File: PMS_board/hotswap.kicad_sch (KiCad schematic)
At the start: 18 parts, among them Q1 Q_NMOS_GDS, Q2 Q_NMOS_GDS, Q3 Q_NMOS_GDS, Q4 Q_NMOS_GDS, U6 LM74800QDRRRQ1, U7 LM74800QDRRRQ1

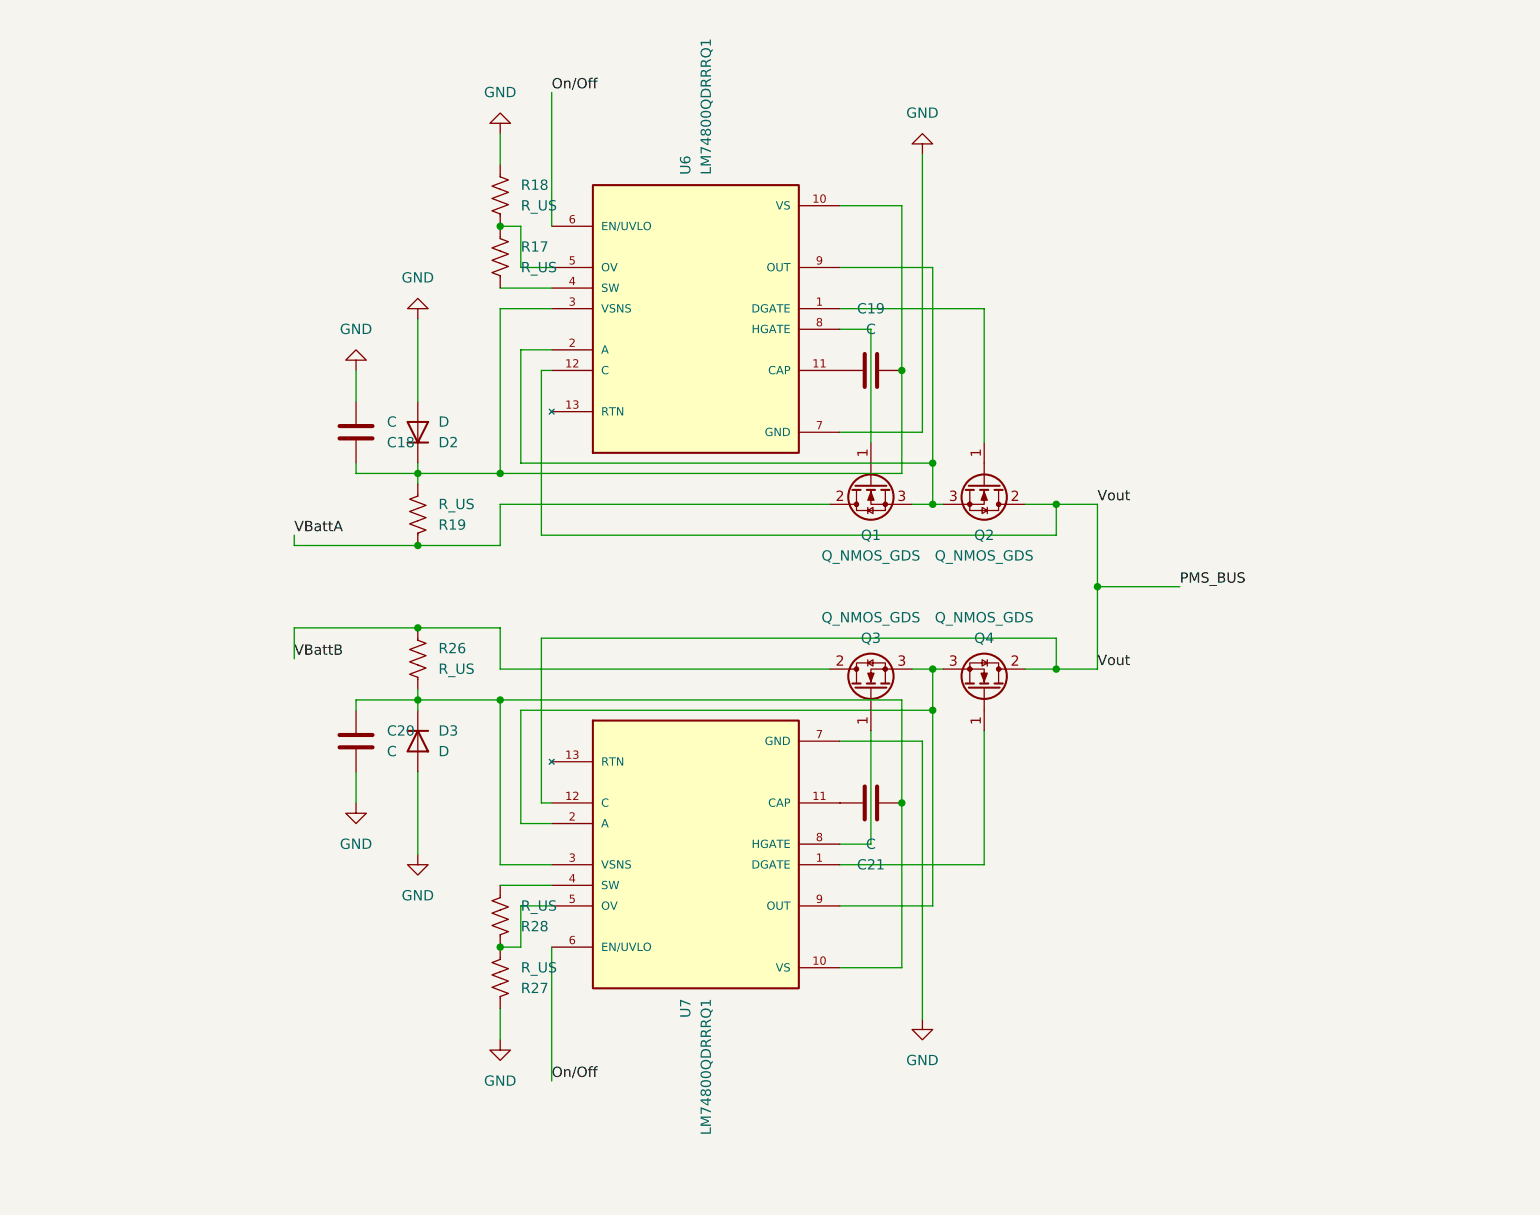
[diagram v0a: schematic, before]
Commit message: Added extra sheets
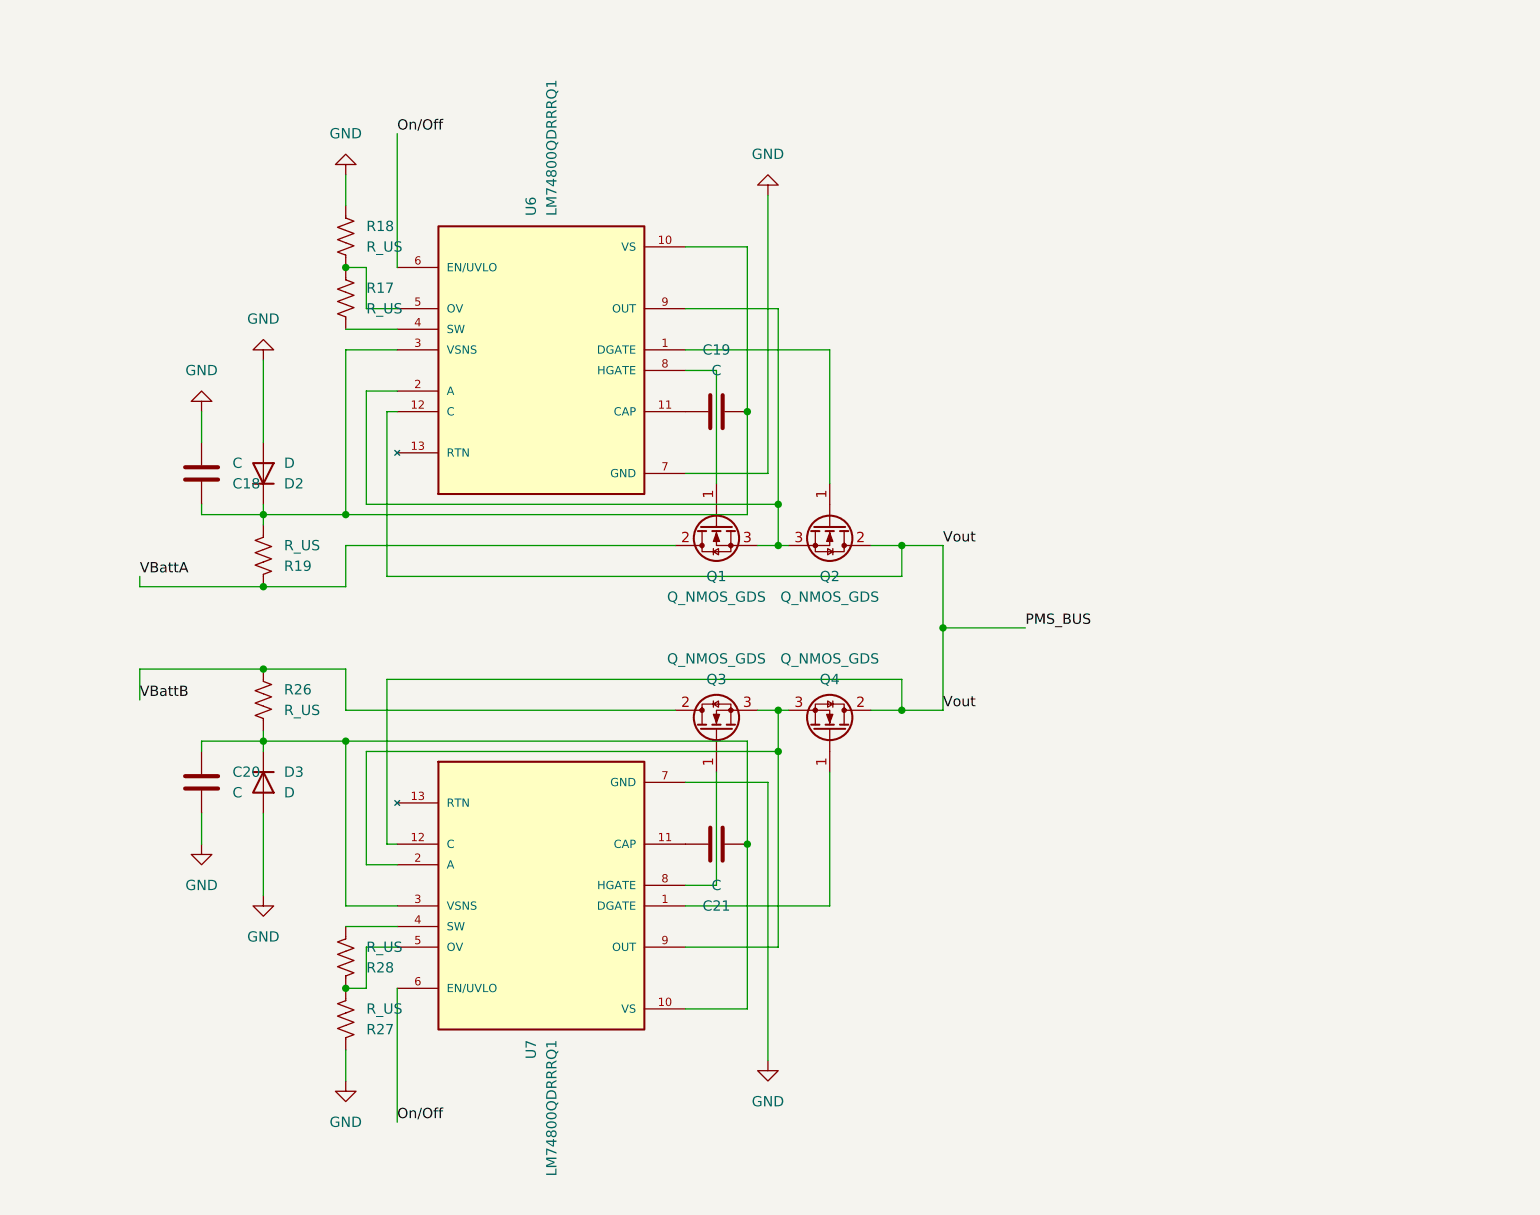
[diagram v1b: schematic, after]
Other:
- moved on the sheet: C18, C19, C20, C21, D2, D3, Q1, Q2, Q3, Q4, R17, R18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

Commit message: Revert "Reapply "progress made :)""
This reverts commit d1e2932f9c3cdbb21c2c39973e18eebc9d543e4e.
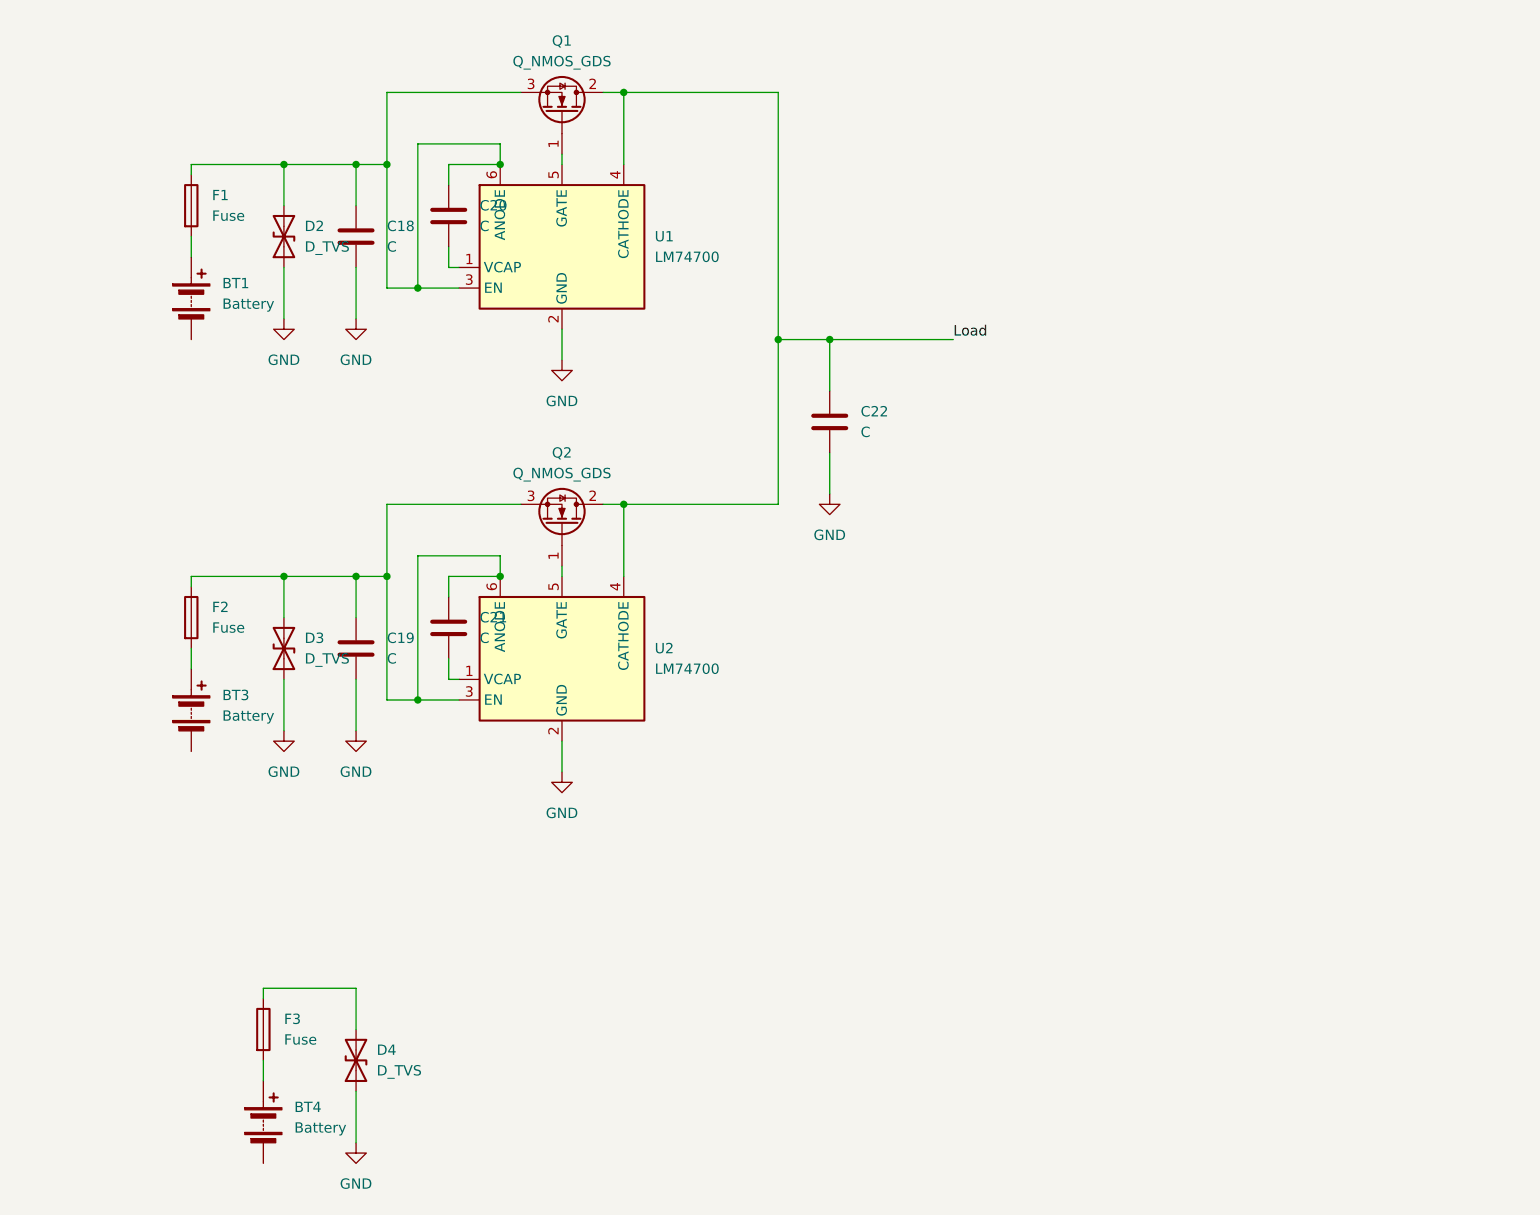
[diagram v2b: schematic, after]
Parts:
- removed D2, D3: D, symbol Device:D
- removed Q3, Q4: Q_NMOS_GDS, symbol Transistor_FET:Q_NMOS_GDS
- removed R17, R18, R19, R26, R27, R28: R_US, symbol Device:R_US
- removed U6, U7: LM74800QDRRRQ1, LM74800QDRRRQ1:IC_LM74800QDRRRQ1, symbol LM74800QDRRRQ1:LM74800QDRRRQ1
- added BT1, BT3, BT4: Battery, symbol Device:Battery
- added C22: C, symbol Device:C
- added D2, D3, D4: D_TVS, symbol Device:D_TVS
- added F1, F2, F3: Fuse, symbol Device:Fuse
- added U1, U2: LM74700, Package_TO_SOT_SMD:SOT-23-6, symbol Power_Management:LM74700
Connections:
- net VBattA is gone; now on net Load: Q1.2 (D)
- net GND: now also C19.2, C22.2, D2.1 (A1), D3.1 (A1), D4.1 (A1), U1.2 (GND), U2.2 (GND); no longer C20.2
- net at C18.1: now also C20.1, Q1.3 (S), D2.2 (A2), F1.1, U1.3 (EN), U1.6 (ANODE); no longer C19.2
- net at Q2.1 (G): now also U2.5 (GATE)
- net at Q2.3 (S): now also C19.1, C21.1, D3.2 (A2), F2.1, U2.3 (EN), U2.6 (ANODE); no longer Q1.3 (S)
- net at C21.2: now also U2.1 (VCAP); no longer C20.1
- net at Q1.1 (G): now also U1.5 (GATE)
- net PMS_BUS renamed Load
- net Load: now also C22.1, U1.4 (CATHODE), U2.4 (CATHODE)
- new net: D4.2 (A2), F3.1
- new net: BT1.1 (+), F1.2
- new net: C20.2, U1.1 (VCAP)
- new net: BT3.1 (+), F2.2
- new net: BT4.1 (+), F3.2

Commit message: progress made :)
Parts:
- removed BT1, BT3, BT4: Battery, symbol Device:Battery
- removed C22: C, symbol Device:C
- removed D2, D3, D4: D_TVS, symbol Device:D_TVS
- removed F1, F2, F3: Fuse, symbol Device:Fuse
- removed U1, U2: LM74700, Package_TO_SOT_SMD:SOT-23-6, symbol Power_Management:LM74700
- added D2, D3: D, symbol Device:D
- added Q3, Q4: Q_NMOS_GDS, symbol Transistor_FET:Q_NMOS_GDS
- added R17, R18, R19, R26, R27, R28: R_US, symbol Device:R_US
- added U6, U7: LM74800QDRRRQ1, LM74800QDRRRQ1:IC_LM74800QDRRRQ1, symbol LM74800QDRRRQ1:LM74800QDRRRQ1
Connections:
- net GND: now also C20.2, D2.2 (A), D3.2 (A), R18.1, R27.1, U6.7 (GND), U7.7 (GND); no longer C19.2
- net at C21.2: now also C20.1, D3.1 (K), R26.2, U7.10 (VS), U7.3 (VSNS)
- net at Q2.1 (G): now also U6.1 (DGATE)
- net at Q1.1 (G): now also U6.8 (HGATE)
- net Load renamed PMS_BUS
- net PMS_BUS: now also Q4.2 (D), U6.12 (C), U7.12 (C); no longer Q1.2 (D)
- new net: Q4.1 (G), U7.1 (DGATE)
- new net: Q3.3 (S), Q4.3 (S), U7.2 (A), U7.9 (OUT)
- new net: C18.1, C19.2, D2.1 (K), R19.2, U6.10 (VS), U6.3 (VSNS)
- new net: Q1.3 (S), Q2.3 (S), U6.2 (A), U6.9 (OUT)
- new net: R17.1, R18.2, U6.5 (OV)
- new net: C19.1, U6.11 (CAP)
- new net: R17.2, U6.4 (SW)
- new net: Q3.1 (G), U7.8 (HGATE)
- new net: C21.1, U7.11 (CAP)
- new net: R28.2, U7.4 (SW)
- new net: R27.2, R28.1, U7.5 (OV)
- new net On/Off: U6.6 (EN/UVLO), U7.6 (EN/UVLO)
- new net VBattA: Q1.2 (D), R19.1
- new net VBattB: Q3.2 (D), R26.1

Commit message: worked on HotSwap
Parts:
- removed C18, C19: C, symbol Device:C
- removed D2: D, symbol Device:D
- removed Q1, Q2: Q_NMOS_GDS, symbol Transistor_FET:Q_NMOS_GDS
- removed R17, R18, R19: R_US, symbol Device:R_US
- removed U6: LM74800QDRRRQ1, LM74800QDRRRQ1:IC_LM74800QDRRRQ1, symbol LM74800QDRRRQ1:LM74800QDRRRQ1
- added C1: 47uF, symbol Device:C_Polarized_US
- added C22: 0.1uF, symbol Device:C
- added C23: 1uF, symbol Device:C
- added D1: SD24C-01F, Diode_SMD:D_SOD-323, symbol Diode:SD24C-01F
- added D4: D, symbol Device:D
- C20: value C -> 1uF
- C21: value C -> 0.1uF
- R26: value R_US -> 10k
- R27: value R_US -> 3.48k
- R28: value R_US -> 100k
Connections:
- net VBattB is gone; now on net Find Clamp!: Q3.2 (D), R26.1
- net GND: now also C1.2, C22.2, C23.1, D1.1 (A1)
- net at Q3.3 (S), Q4.3 (S), U7.2 (A)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: now also C23.2
- net at C20.1, C21.2, D3.1 (K)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: now also U7.4 (SW)
- net Find Clamp!: now reaches R28.2
- net Find Clamp!: now also C22.1, D4.1 (K); no longer U7.4 (SW)
- net PMS_BUS renamed Ask about v/out clamp
- net Ask about v/out clamp: now also C1.1
- new net: D1.2 (A2), D4.2 (A)

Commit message: added buzzer? looked into stuff
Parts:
- added C24, C26: 0.1uF, symbol Device:C
- added C25, C27: 1uF, symbol Device:C
- added C6: 47uF, symbol Device:C_Polarized_US
- added D2: SD24C-01F, Diode_SMD:D_SOD-323, symbol Diode:SD24C-01F
- added D5, D8: D, symbol Device:D
- added Q11, Q12: Q_NMOS_GDS, symbol Transistor_FET:Q_NMOS_GDS
- added R29: 10k, symbol Device:R_US
- added R30: 100k, symbol Device:R_US
- added R31: 3.48k, symbol Device:R_US
- added U12: LM74800QDRRRQ1, LM74800QDRRRQ1:IC_LM74800QDRRRQ1, symbol LM74800QDRRRQ1:LM74800QDRRRQ1
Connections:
- net Ask about v/out clamp: now also C6.1, Q12.2 (D), U12.12 (C)
- net Find Clamp!: now also C24.1, D5.1 (K), Q11.2 (D), R29.1, R30.2
- net GND: now also C24.2, C25.2, C27.1, C6.2, D2.1 (A1), D8.2 (A), R31.1, U12.7 (GND)
- net On/Off: now also U12.6 (EN/UVLO)
- new net: C26.1, U12.11 (CAP)
- new net: C25.1, C26.2, D8.1 (K), R29.2, U12.10 (VS), U12.3 (VSNS), U12.4 (SW)
- new net: C27.2, Q11.3 (S), Q12.3 (S), U12.2 (A), U12.9 (OUT)
- new net: R30.1, R31.2, U12.5 (OV)
- new net: Q12.1 (G), U12.1 (DGATE)
- new net: Q11.1 (G), U12.8 (HGATE)
- new net: D2.2 (A2), D5.2 (A)
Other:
- moved on the sheet: C1, C20, C21, C22, C23, D1, D3, D4, Q3, Q4, R26, R27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

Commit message: Fix Hotswap
I fixed hotswap, i think :)
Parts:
- removed C1, C6: 47uF, symbol Device:C_Polarized_US
- removed C20, C25: 1uF, symbol Device:C
- removed C21, C24, C26: 0.1uF, symbol Device:C
- removed D1, D2: SD24C-01F, Diode_SMD:D_SOD-323, symbol Diode:SD24C-01F
- removed D3, D8: D, symbol Device:D
- removed Q11, Q12, Q3, Q4: Q_NMOS_GDS, symbol Transistor_FET:Q_NMOS_GDS
- removed R26: 10k, symbol Device:R_US
- removed R27: 3.48k, symbol Device:R_US
- removed R28: 100k, symbol Device:R_US
- removed U7: LM74800QDRRRQ1, LM74800QDRRRQ1:IC_LM74800QDRRRQ1, symbol LM74800QDRRRQ1:LM74800QDRRRQ1
- added C40, C42: 1uF, symbol Device:C
- added C41, C43: 47uF, symbol Device:C_Polarized_US
- added C44: 0.1uF, symbol Device:C
- added Q5, Q6, Q7, Q8: Q_NMOS_GDS, symbol Transistor_FET:Q_NMOS_GDS
- added R36: 10k, symbol Device:R_US
- added R37: 100k, symbol Device:R_US
- added R38: 3.48k, symbol Device:R_US
- added U9: LM74800QDRRRQ1, LM74800QDRRRQ1:IC_LM74800QDRRRQ1, symbol LM74800QDRRRQ1:LM74800QDRRRQ1
- C22: value 0.1uF -> 1uF
- C27: value 1uF -> 0.1uF
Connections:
- net On/Off is gone; now on an unnamed net: U12.6 (EN/UVLO)
- net GND: now also C23.2, D4.2 (A), D5.2 (A), C40.2, C41.2, C42.2, C43.2, R38.1, U9.7 (GND); no longer C23.1, C27.1
- net at U12.11 (CAP): now also C44.1
- net at U12.10 (VS), U12.3 (VSNS): now also C23.1, D5.1 (K), C44.2, R36.2; no longer R29.2, U12.4 (SW)
- net at U12.2 (A), U12.9 (OUT): now also C42.1, Q7.3 (S), Q8.3 (S); no longer C27.2
- net at R30.1, R31.2: now also U9.5 (OV); no longer U12.5 (OV)
- net at U12.1 (DGATE): now also Q7.1 (G)
- net at U12.8 (HGATE): now also Q8.1 (G)
- net Ask about v/out clamp: no longer names the net of U12.12 (C)
- net Ask about v/out clamp: now also C43.1, Q7.2 (D)
- removed net Find Clamp!: C22.1, D4.1 (K), D5.1 (K), R29.1, R30.2
- new net: R37.1, R38.2, U12.5 (OV)
- new net: R37.2, U12.4 (SW)
- new net: R30.2, U9.4 (SW)
- new net: C27.1, U9.11 (CAP)
- new net: C22.1, C27.2, D4.1 (K), R29.2, U9.10 (VS), U9.3 (VSNS), U9.6 (EN/UVLO)
- new net: Q6.1 (G), U9.1 (DGATE)
- new net: C41.1, Q6.2 (D), U9.12 (C)
- new net: C40.1, Q5.3 (S), Q6.3 (S), U9.2 (A), U9.9 (OUT)
- new net: Q5.1 (G), U9.8 (HGATE)
- new net BattA: Q8.2 (D), R36.1
- new net BattB: Q5.2 (D), R29.1
